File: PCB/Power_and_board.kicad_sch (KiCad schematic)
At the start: 21 parts, among them U5 AMS1117-3.3

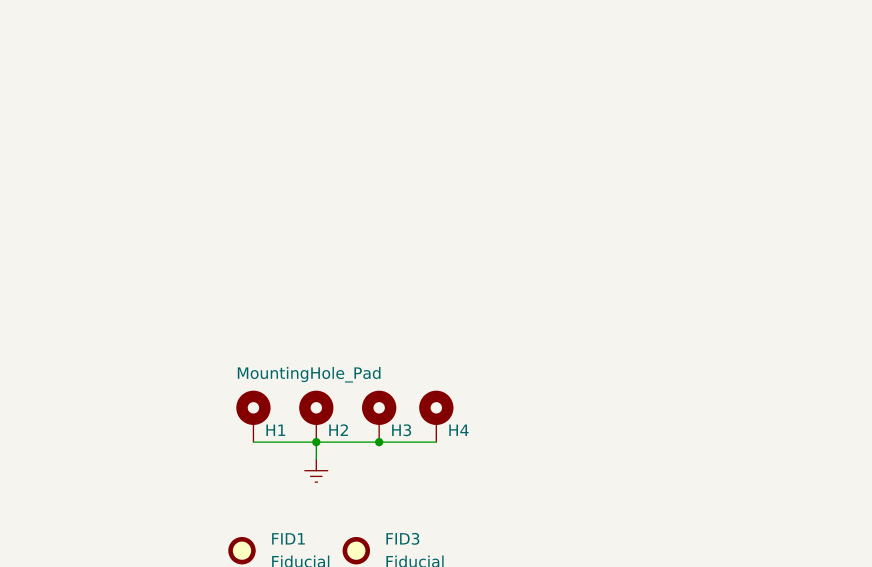
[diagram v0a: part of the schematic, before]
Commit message: changed mounting holes to ones without fiducials and fixed power calculation
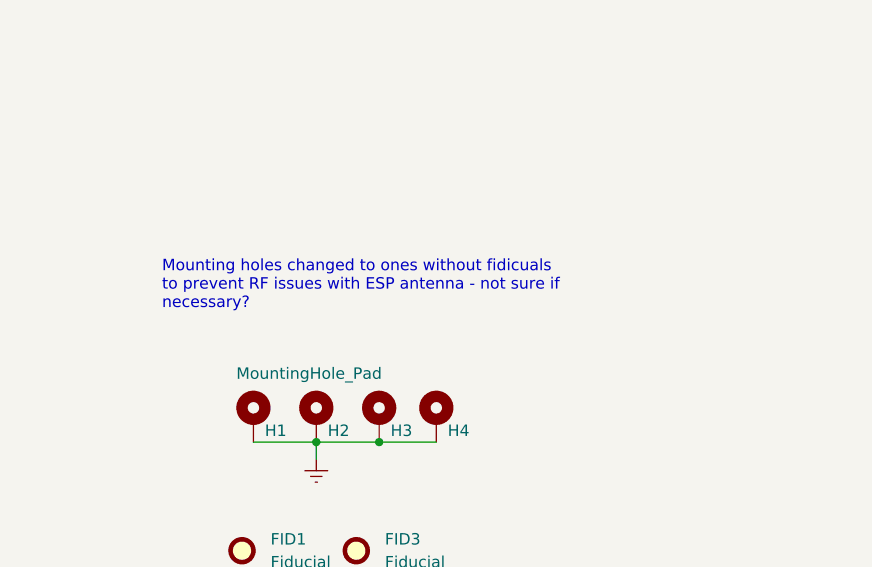
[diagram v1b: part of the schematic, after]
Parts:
- H1, H2, H3, H4: footprint MountingHole:MountingHole_2.2mm_M2_Pad_Via -> MountingHole:MountingHole_2.2mm_M2_ISO7380
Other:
- note added: "Mounting holes changed to ones without fidicuals to prevent RF issues with ESP antenna - not sure if necessary?"
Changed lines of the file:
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@@
     (effects (font (size 2.2 2.2) (thickness 0.44) bold) (justify left bottom))
+  )
+  (text "Mounting holes changed to ones without fidicuals \nto prevent RF issues with ESP antenna - not sure if \nnecessary?"
+    (at 140.97 158.75 0)
+    (effects (font (size 1.27 1.27)) (justify left bottom))
   )
   (label "12VDC IN" (at 121.92 94.615 0) (fields_autoplaced)
@@
       (effects (font (size 1.27 1.27)) (justify left) hide)
     )
-    (property "Footprint" "MountingHole:MountingHole_2.2mm_M2_Pad_Via" (at 165.1 170.815 0)
+    (property "Footprint" "MountingHole:MountingHole_2.2mm_M2_ISO7380" (at 165.1 170.815 0)
       (effects (font (size 1.27 1.27)) hide)
     )
@@
       (effects (font (size 1.27 1.27)) (justify left) hide)
     )
-    (property "Footprint" "MountingHole:MountingHole_2.2mm_M2_Pad_Via" (at 171.45 170.815 0)
+    (property "Footprint" "MountingHole:MountingHole_2.2mm_M2_ISO7380" (at 171.45 170.815 0)
       (effects (font (size 1.27 1.27)) hide)
     )
@@
       (effects (font (size 1.27 1.27)) (justify left))
     )
-    (property "Footprint" "MountingHole:MountingHole_2.2mm_M2_Pad_Via" (at 151.13 170.815 0)
+    (property "Footprint" "MountingHole:MountingHole_2.2mm_M2_ISO7380" (at 151.13 170.815 0)
       (effects (font (size 1.27 1.27)) hide)
     )
@@
       (effects (font (size 1.27 1.27)) (justify left) hide)
     )
-    (property "Footprint" "MountingHole:MountingHole_2.2mm_M2_Pad_Via" (at 158.115 170.815 0)
-      (effects (font (size 1.27 1.27)) hide)
-    )
+    (property "Footprint" "MountingHole:MountingHole_2.2mm_M2_ISO7380" (at 158.115 170.815 0)
+      (effects (font (size 1.27 1.27)) hide)
+    )

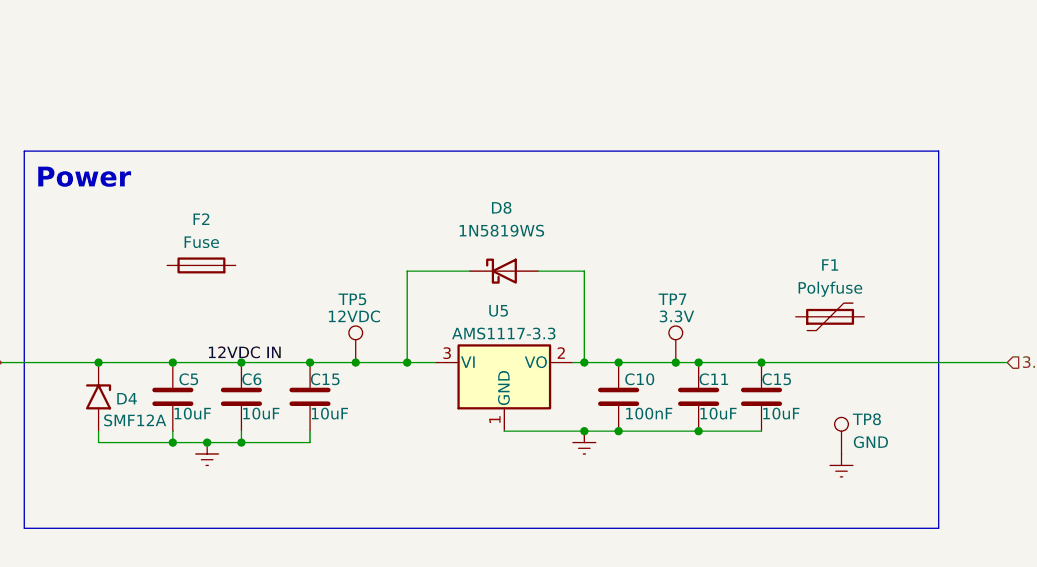
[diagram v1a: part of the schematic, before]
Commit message: Redesign around new components added to scheamtic
 - shift left most of board
 - re-layout
 - new components
 - drc passes (mostly)
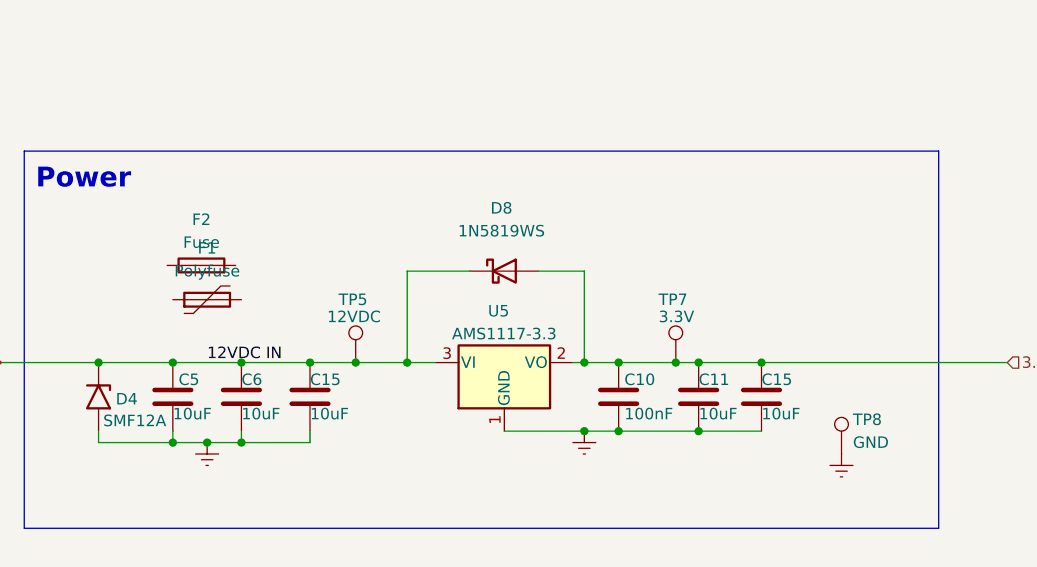
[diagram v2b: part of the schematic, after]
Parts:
- H1, H3, H4: footprint MountingHole:MountingHole_2.2mm_M2_ISO7380 -> MountingHole:MountingHole_2.2mm_M2_Pad_Via
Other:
- moved on the sheet: F1
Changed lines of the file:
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@@
       (effects (font (size 1.27 1.27)) (justify left) hide)
     )
-    (property "Footprint" "MountingHole:MountingHole_2.2mm_M2_ISO7380" (at 165.1 170.815 0)
+    (property "Footprint" "MountingHole:MountingHole_2.2mm_M2_Pad_Via" (at 165.1 170.815 0)
       (effects (font (size 1.27 1.27)) hide)
     )
@@
     )
   )
-  (symbol (lib_id "Device:Polyfuse") (at 191.135 89.535 90) (unit 1)
+  (symbol (lib_id "Device:Polyfuse") (at 121.92 87.63 90) (unit 1)
     (in_bom yes) (on_board yes) (dnp no) (fields_autoplaced)
-    (property "Reference" "F1" (at 191.135 83.82 90)
-      (effects (font (size 1.27 1.27)))
-    )
-    (property "Value" "Polyfuse" (at 191.135 86.36 90)
-      (effects (font (size 1.27 1.27)))
-    )
-    (property "Footprint" "" (at 196.215 88.265 0)
+    (property "Reference" "F1" (at 121.92 81.915 90)
+      (effects (font (size 1.27 1.27)))
+    )
+    (property "Value" "Polyfuse" (at 121.92 84.455 90)
+      (effects (font (size 1.27 1.27)))
+    )
+    (property "Footprint" "" (at 127 86.36 0)
       (effects (font (size 1.27 1.27)) (justify left) hide)
     )
-    (property "Datasheet" "~" (at 191.135 89.535 0)
-      (effects (font (size 1.27 1.27)) hide)
-    )
-    (property "Description" "I think this one? https://www.lcsc.com/product-detail/Resettable-Fuses_BOURNS-MF-MSMF075-2_C84140.html" (at 191.135 89.535 90)
+    (property "Datasheet" "~" (at 121.92 87.63 0)
+      (effects (font (size 1.27 1.27)) hide)
+    )
+    (property "Description" "I think this one? https://www.lcsc.com/product-detail/Resettable-Fuses_BOURNS-MF-MSMF075-2_C84140.html" (at 121.92 87.63 90)
       (effects (font (size 1.27 1.27)) hide)
     )
@@
       (effects (font (size 1.27 1.27)) (justify left) hide)
     )
-    (property "Footprint" "MountingHole:MountingHole_2.2mm_M2_ISO7380" (at 171.45 170.815 0)
+    (property "Footprint" "MountingHole:MountingHole_2.2mm_M2_Pad_Via" (at 171.45 170.815 0)
       (effects (font (size 1.27 1.27)) hide)
     )
@@
       (effects (font (size 1.27 1.27)) (justify left))
     )
-    (property "Footprint" "MountingHole:MountingHole_2.2mm_M2_ISO7380" (at 151.13 170.815 0)
-      (effects (font (size 1.27 1.27)) hide)
-    )
+    (property "Footprint" "MountingHole:MountingHole_2.2mm_M2_Pad_Via" (at 151.13 170.815 0)
+      (effects (font (size 1.27 1.27)) hide)
+    )
